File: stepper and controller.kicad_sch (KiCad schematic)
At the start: 30 parts

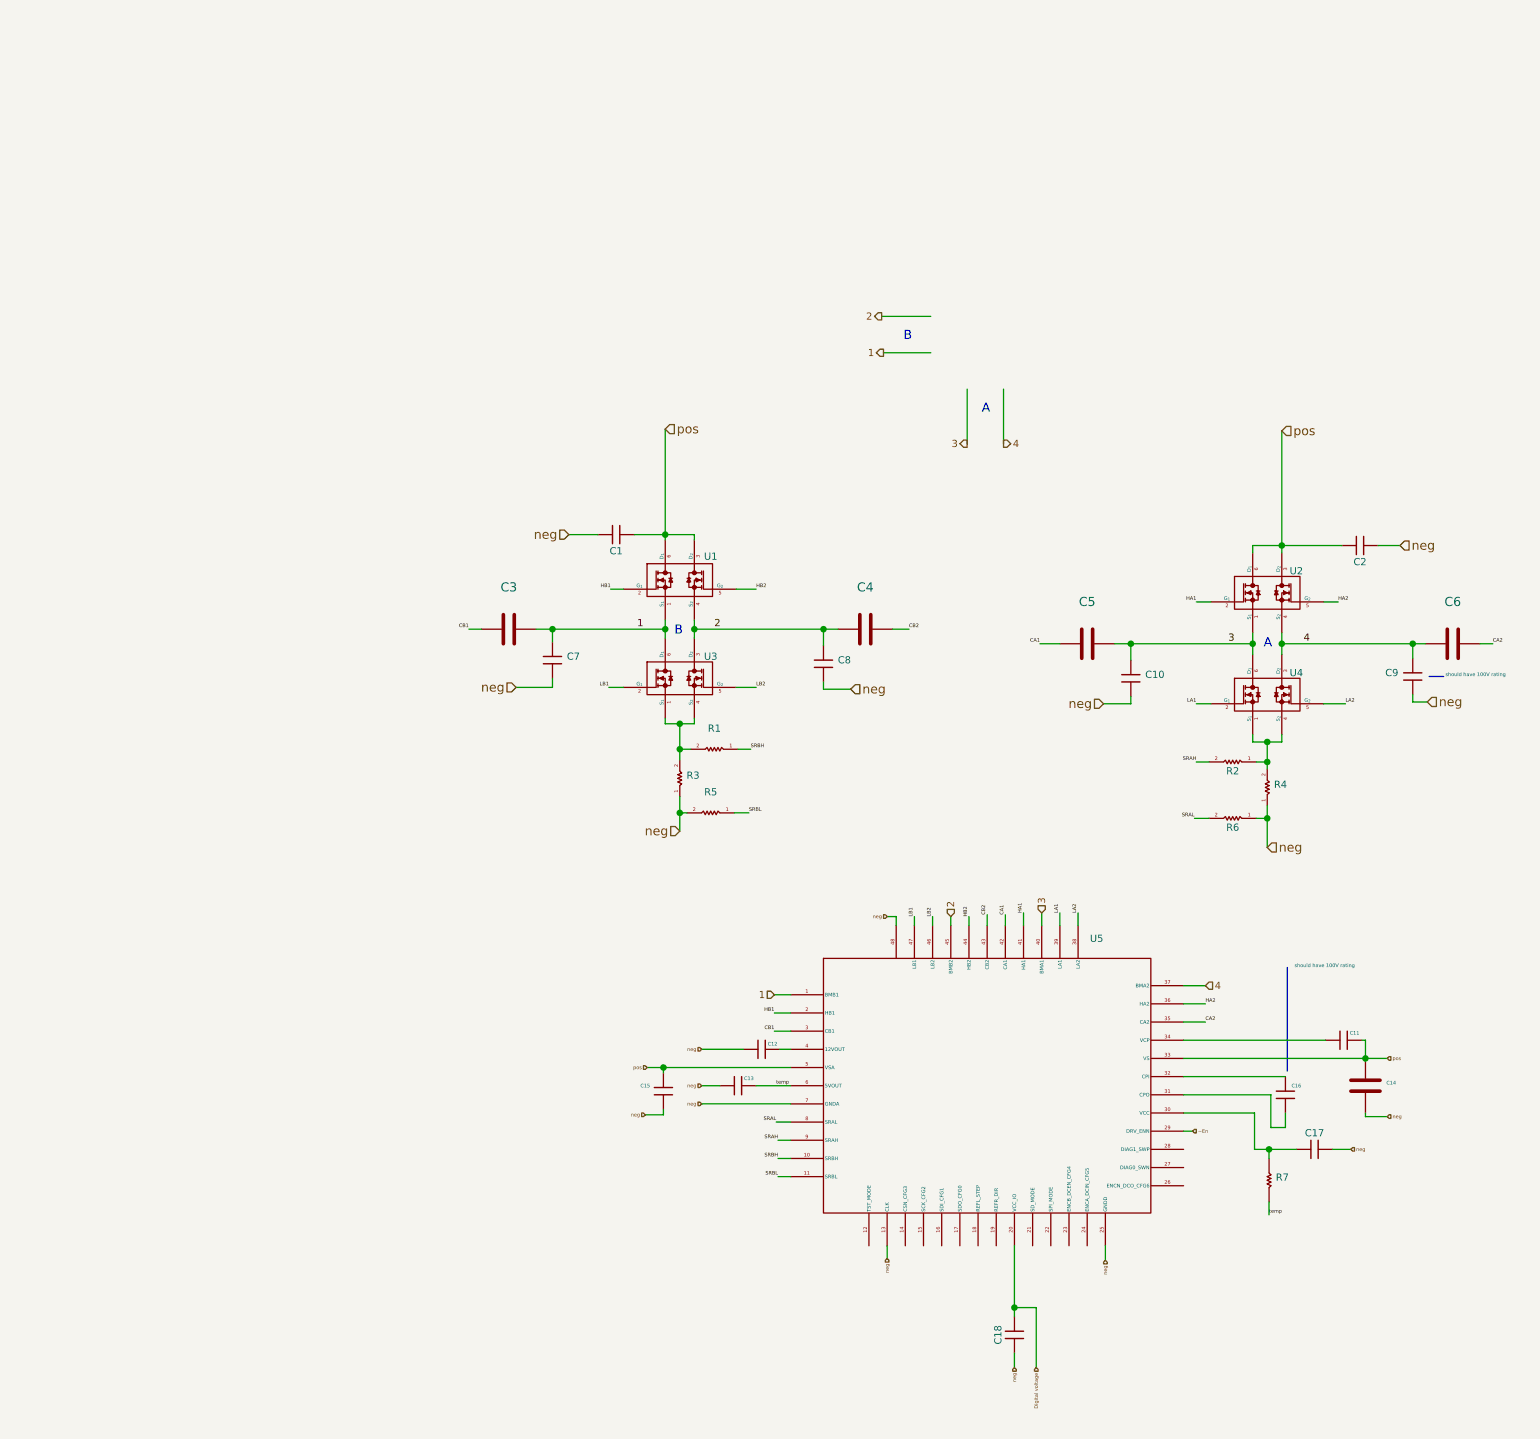
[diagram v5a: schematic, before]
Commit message: make a TH version of the base PCB for testing purposes...
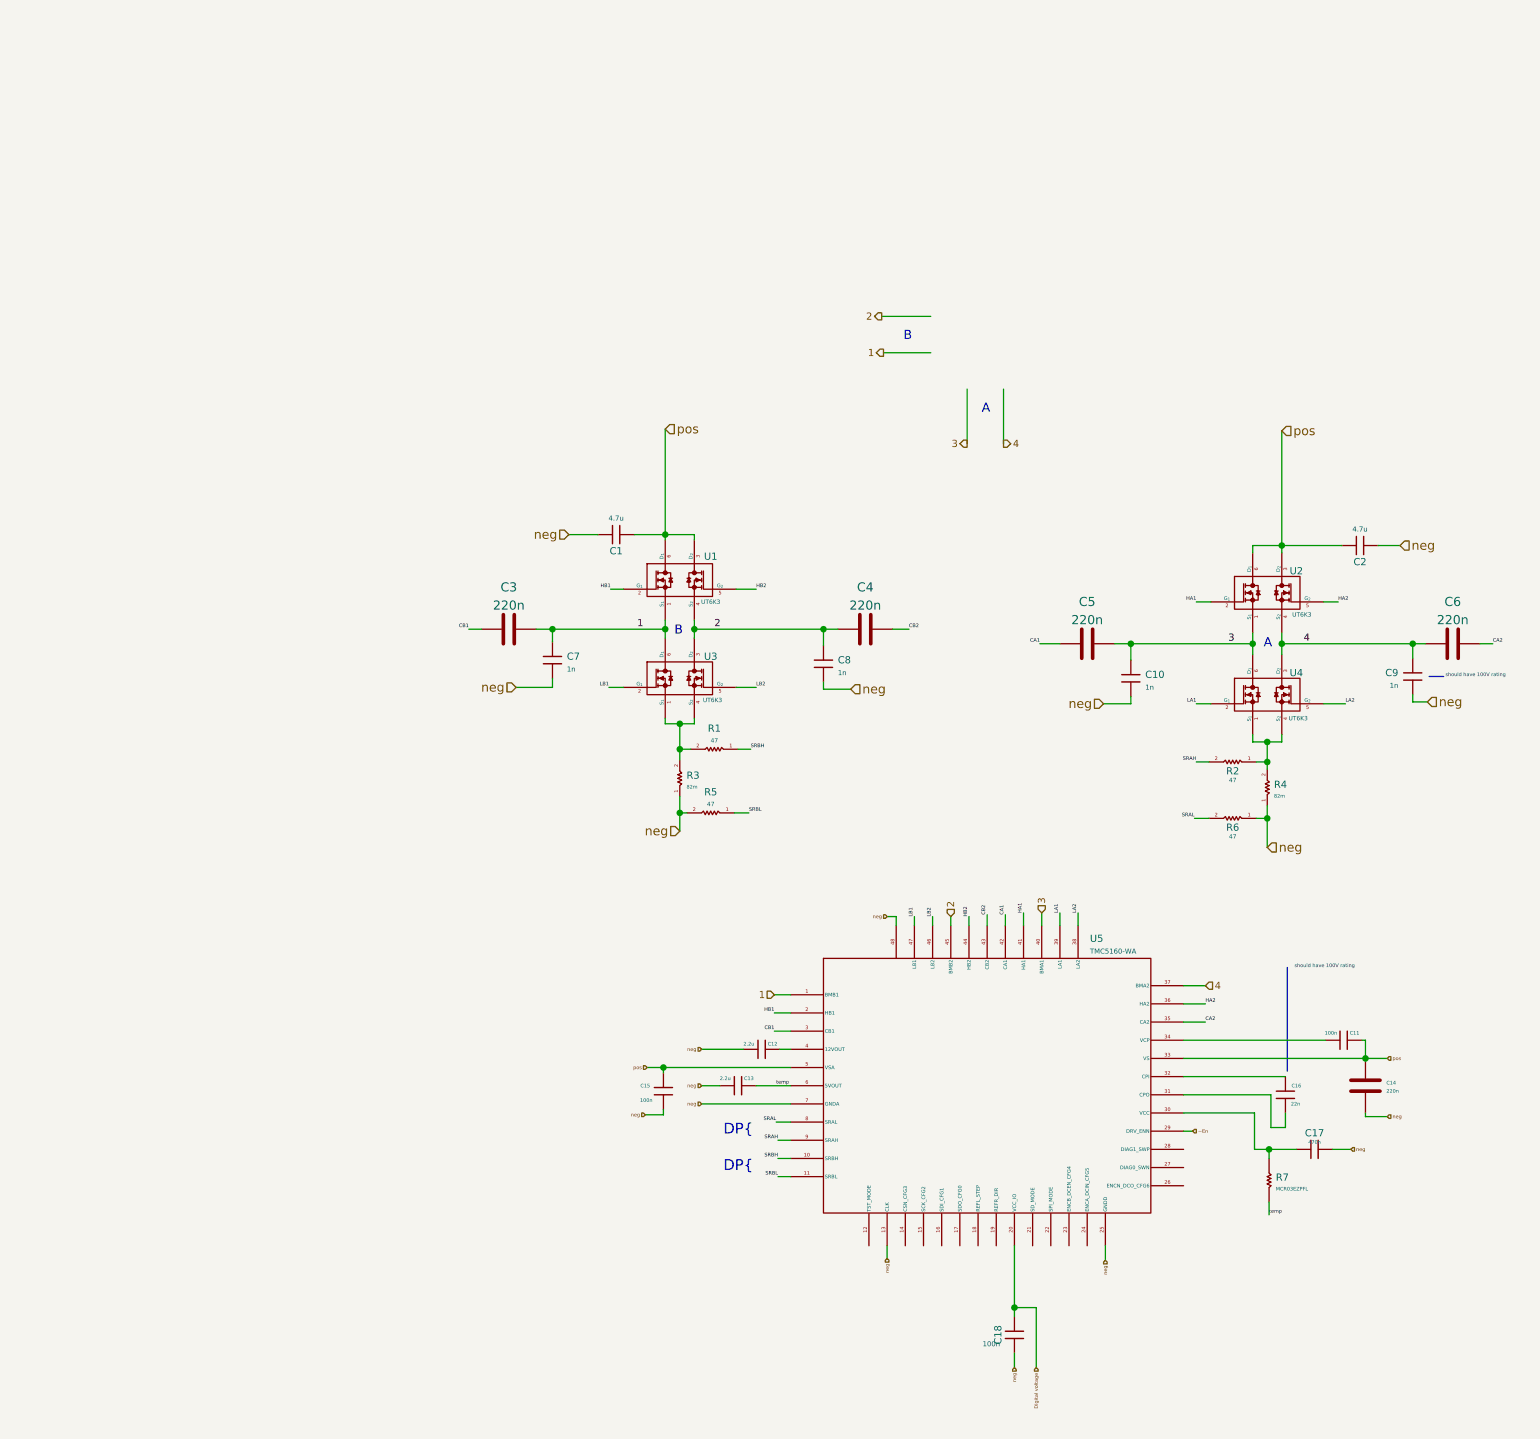
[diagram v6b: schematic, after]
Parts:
- C1, C2: value (none) -> 4.7u; footprint (none) -> Capacitors:C0603X105J4RACTU
- C10, C7, C8, C9: value (none) -> 1n; footprint (none) -> Capacitors:C0603X105J4RACTU
- C11, C15, C18: value (none) -> 100n; footprint (none) -> Capacitors:C0603X105J4RACTU
- C12, C13: value (none) -> 2.2u; footprint (none) -> Capacitors:C0603X105J4RACTU
- C14, C3, C4, C5, C6: value (none) -> 220n; footprint (none) -> Capacitors:C0603X105J4RACTU
- C16: value (none) -> 22n; footprint (none) -> Capacitors:C0603X105J4RACTU
- C17: value (none) -> 470n; footprint (none) -> Capacitors:C0603X105J4RACTU
- R1, R2, R5, R6: value (none) -> 47; footprint (none) -> Resistors:MCR03EZPFX
- R3, R4: value (none) -> 82m; footprint (none) -> Resistors:GMR50HJBFWR082
- R7: value (none) -> MCR03EZPFL; footprint (none) -> Resistors:MCR03EZPFL
- U1, U2, U3, U4: value (none) -> UT6K3; footprint (none) -> E-MOSFETs:UT6K3TCR
- U5: value (none) -> TMC5160-WA; footprint (none) -> ICs:TMC5160-WA
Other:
- note added: "DP{"
